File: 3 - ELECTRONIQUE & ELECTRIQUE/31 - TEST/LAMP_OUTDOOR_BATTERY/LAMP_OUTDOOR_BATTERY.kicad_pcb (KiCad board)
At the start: 2 copper layers, 15.3 x 61.6 mm, 13 parts, among them J1 629722000214, U1 MCP73833-FCI_UN, U2 MT3608

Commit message: Commit_1.02 Modification shape PCB
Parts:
- C1, C2: footprint Capacitor_SMD:C_0805_2012Metric_Pad1.18x1.45mm_HandSolder -> Capacitor_SMD:C_0402_1005Metric_Pad0.74x0.62mm_HandSolder
- R1, R2, R3, R4, R5: footprint Resistor_SMD:R_0805_2012Metric_Pad1.20x1.40mm_HandSolder -> Resistor_SMD:R_0402_1005Metric_Pad0.72x0.64mm_HandSolder
- moved C1 45.7 mm to (187.9, 79.4)
- moved C2 45.7 mm to (187.9, 82.4)
- moved D1 45.7 mm to (183.2, 79.4)
- moved D2 45.7 mm to (183.2, 82.4)
- moved D3 45.7 mm to (183.2, 85.5)
- moved U1 45.7 mm to (186.2, 74.4)
- moved R1 45.3 mm to (187.6, 104.4)
- moved R2 45.3 mm to (187.6, 107.4)
- moved R3 45.3 mm to (187.6, 110.3)
- moved R4 45.3 mm to (187.6, 113.3)
- moved R5 45.3 mm to (187.6, 116.2)
- moved U2 45.3 mm to (185.1, 99.8)
- moved J1 41.5 mm to (170.5, 91.5)
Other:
- board size 15.3 x 61.6 mm -> 24.5 x 67.8 mm

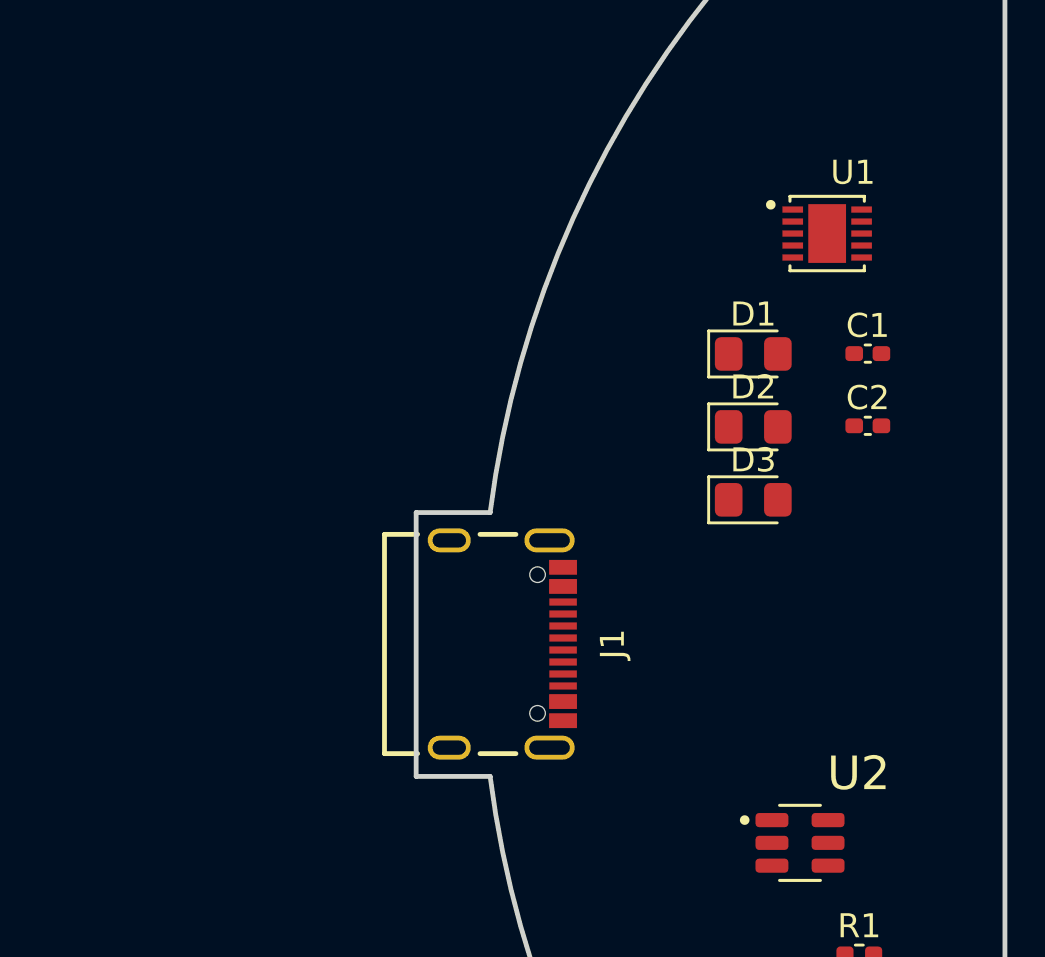
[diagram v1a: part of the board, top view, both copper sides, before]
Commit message: Boost converter circuit
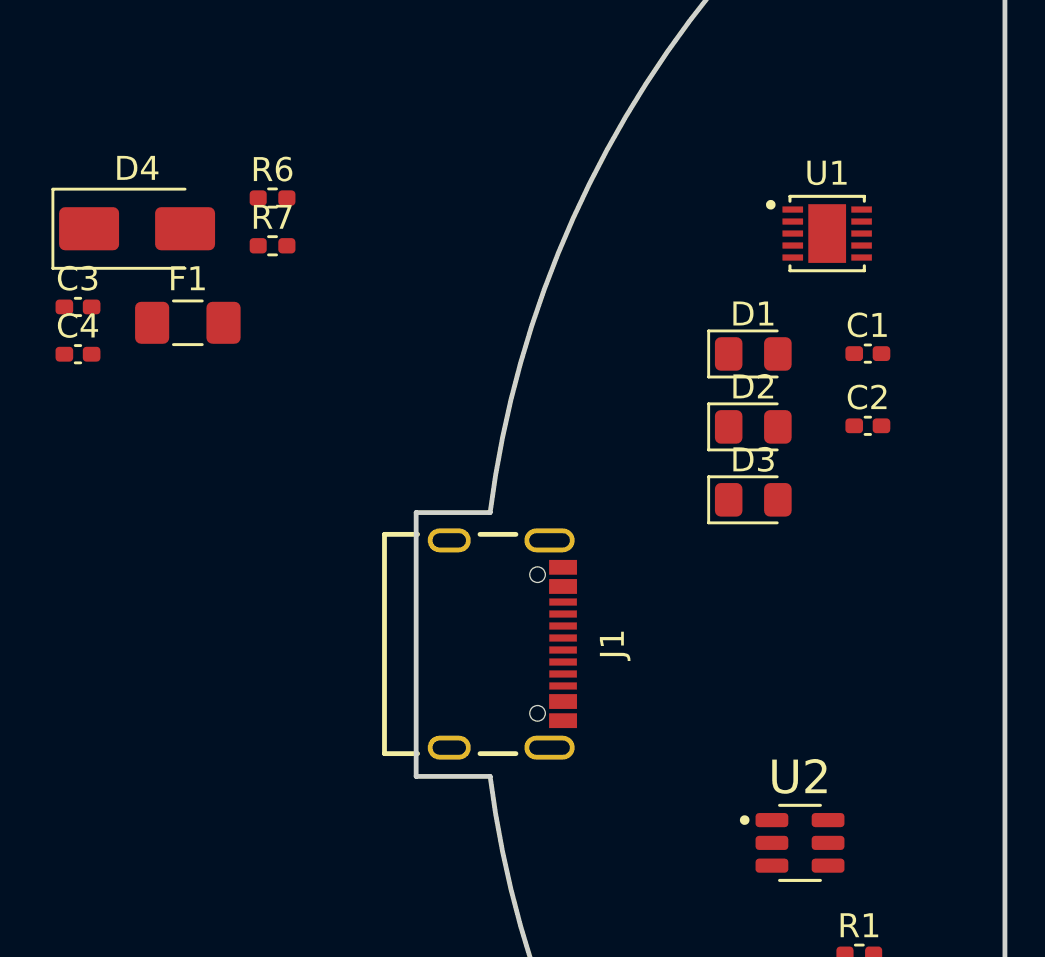
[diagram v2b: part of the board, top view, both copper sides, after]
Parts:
- added C3: 22uF, Capacitor_SMD:C_0402_1005Metric_Pad0.74x0.62mm_HandSolder, F.Cu at (155.0, 77.4)
- added C4: 22uF, Capacitor_SMD:C_0402_1005Metric_Pad0.74x0.62mm_HandSolder, F.Cu at (155.0, 79.4)
- added D4: SS24, Diode_SMD:D_SMA, F.Cu at (157.5, 74.2)
- added F1: Fuse_Small, Fuse:Fuse_1206_3216Metric_Pad1.42x1.75mm_HandSolder, F.Cu at (159.6, 78.1)
- added R6: 110K, Resistor_SMD:R_0402_1005Metric_Pad0.72x0.64mm_HandSolder, F.Cu at (163.1, 72.9)
- added R7: 15K, Resistor_SMD:R_0402_1005Metric_Pad0.72x0.64mm_HandSolder, F.Cu at (163.1, 74.9)
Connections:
- U2 pad 1: unconnected-(U2-SW-Pad1) -> Net-(D4-A)
- U2 pad 2: unconnected-(U2-GND-Pad2) -> GND
- U2 pad 3: unconnected-(U2-FB-Pad3) -> Net-(U2-FB)
- U2 pad 5: unconnected-(U2-IN-Pad5) -> +BATT

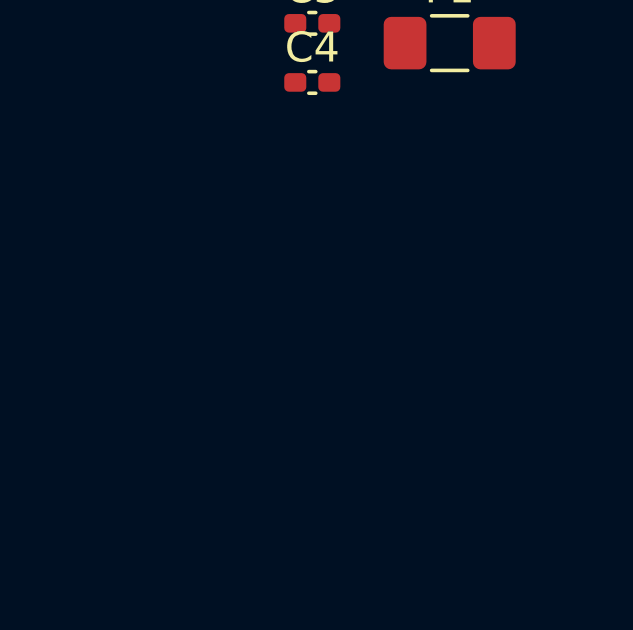
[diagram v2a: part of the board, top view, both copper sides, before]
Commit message: Import des symboles et empreintes
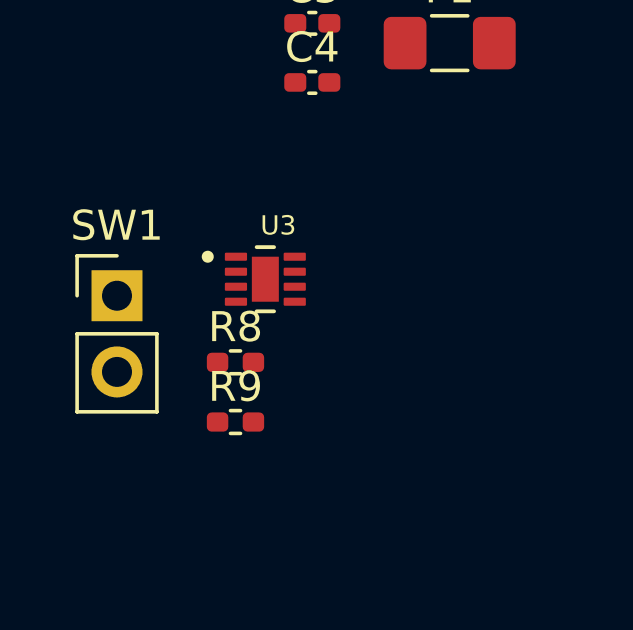
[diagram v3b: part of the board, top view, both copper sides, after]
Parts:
- added R8: 10K, Resistor_SMD:R_0402_1005Metric_Pad0.72x0.64mm_HandSolder, F.Cu at (152.4, 88.7)
- added R9: 10K, Resistor_SMD:R_0402_1005Metric_Pad0.72x0.64mm_HandSolder, F.Cu at (152.4, 90.7)
- added SW1: SW_SPST, Connector_PinHeader_2.54mm:PinHeader_1x02_P2.54mm_Vertical, F.Cu at (148.5, 86.5)
- added U3: AT42QT1012-MAHR, LAMP_OUTDOOR_BATTERY:SON50P200X200X60-9N, F.Cu at (153.4, 86.0)
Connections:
- net Net-(D4-A) renamed /SW
- net Net-(U2-FB) renamed /V_FB
- C3 pad 2: +BATT -> /IN
- F1 pad 1: +BATT -> Net-(BT1-+)
- F1 pad 2: BatteryPole+ -> +BATT
- U2 pad 4: unconnected-(U2-EN-Pad4) -> TS
- U2 pad 5: +BATT -> /IN

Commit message: Conception schéma suite
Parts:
- added C5: ~, Capacitor_SMD:C_0402_1005Metric_Pad0.74x0.62mm_HandSolder, F.Cu at (112.1, 73.0)
- added C6: 0.1uF, Capacitor_SMD:C_0402_1005Metric_Pad0.74x0.62mm_HandSolder, F.Cu at (112.1, 75.0)
- added J2: Batt+, LAMP_OUTDOOR_BATTERY:BatteryPole, F.Cu at (157.6, 60.3)
- added J3: Batt-, LAMP_OUTDOOR_BATTERY:BatteryPole, F.Cu at (157.6, 113.7)
- added L1: 4.7uH, Inductor_SMD:L_0805_2012Metric_Pad1.15x1.40mm_HandSolder, F.Cu at (129.5, 105.5)
- added R10: ~, Resistor_SMD:R_0402_1005Metric_Pad0.72x0.64mm_HandSolder, F.Cu at (108.9, 73.0)
- added R11: ~, Resistor_SMD:R_0402_1005Metric_Pad0.72x0.64mm_HandSolder, F.Cu at (108.9, 75.0)
- added R12: 100k, Resistor_SMD:R_0402_1005Metric_Pad0.72x0.64mm_HandSolder, F.Cu at (108.9, 77.0)
- added R13: 0, Resistor_SMD:R_0402_1005Metric_Pad0.72x0.64mm_HandSolder, F.Cu at (117.9, 63.4)
- moved U3 52.8 mm to (103.9, 104.0)
- moved D3 43.9 mm to (145.8, 108.7), turned to 90 degrees
- moved D2 43.5 mm to (145.8, 104.7), turned to 90 degrees
- moved D1 43.0 mm to (145.8, 100.8), turned to 90 degrees
- moved C1 41.1 mm to (148.4, 90.6), turned to -90 degrees
- moved R5 39.9 mm to (155.6, 92.3)
- moved U2 39.6 mm to (151.8, 78.4)
- moved U1 39.0 mm to (151.4, 91.9)
- moved R1 38.3 mm to (150.2, 96.0), turned to 90 degrees
- moved R2 37.9 mm to (151.4, 96.0), turned to 90 degrees
- moved R3 37.8 mm to (152.6, 96.0), turned to 90 degrees
- moved R4 37.6 mm to (155.6, 93.4)
- moved C2 34.4 mm to (154.5, 90.6), turned to -90 degrees
- moved D4 32.3 mm to (125.2, 74.6)
- moved R6 32.3 mm to (130.8, 73.3)
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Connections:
- F1 pad 1: Net-(BT1-+) -> /Battery+
- R8 pad 1: TS -> /EN
- R9 pad 2: TS -> /EN
- U2 pad 4: TS -> /EN
- U3 pad 1: unconnected-(U3-SNSK-Pad1) -> Net-(U3-SNSK)
- U3 pad 4: unconnected-(U3-VSS-Pad4) -> GND
- U3 pad 5: unconnected-(U3-OUT-Pad5) -> TS
- U3 pad 6: unconnected-(U3-TIME-Pad6) -> GND
- U3 pad 7: unconnected-(U3-VDD-Pad7) -> +5V
- U3 pad 8: unconnected-(U3-SNS-Pad8) -> Net-(U3-SNS)
- U3 pad 9: unconnected-(U3-EXP-Pad9) -> GND
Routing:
- net Net-(U1-STAT1): track 0.00 -> 5.17 mm
- net Net-(U1-STAT2): track 0.00 -> 4.83 mm
- net Net-(U1-~{PG}): track 0.00 -> 4.49 mm, vias 0 -> 2
- net Net-(U1-THERM): track 0.00 -> 2.29 mm
- net Net-(U1-PROG): track 0.00 -> 1.95 mm
- net GND: vias 0 -> 1
- added copper zone on F.Cu, net +5V
- added copper zone on F.Cu, net +BATT
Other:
- board size 24.5 x 67.8 mm -> 24 x 68.3 mm

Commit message: Conception PCB suite
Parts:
- removed F1: Fuse_Small, Fuse:Fuse_1206_3216Metric_Pad1.42x1.75mm_HandSolder
- added ? (x2): , , F.Cu at (157.8, 123.1)
- added C7: 0.1uF, Capacitor_SMD:C_0402_1005Metric_Pad0.74x0.62mm_HandSolder, F.Cu at (149.4, 83.6)
- added J4: Led+, LAMP_OUTDOOR_BATTERY:BatteryPole, F.Cu at (157.4, 110.5)
- added J5: Led-, LAMP_OUTDOOR_BATTERY:BatteryPole, F.Cu at (157.4, 114.5)
- added J6: Electrode Sensor, LAMP_OUTDOOR_BATTERY:BatteryPole, F.Cu at (165.4, 86.1)
- added Q1: IRLML6344, Package_TO_SOT_SMD:SOT-23-3, F.Cu at (146.0, 79.6)
- added Q2: IRLML6344, Package_TO_SOT_SMD:SOT-23-3, F.Cu at (146.0, 83.4)
- added R14: 2.2K, Resistor_SMD:R_0402_1005Metric_Pad0.72x0.64mm_HandSolder, F.Cu at (149.3, 79.3)
- added R15: 330, Resistor_SMD:R_0402_1005Metric_Pad0.72x0.64mm_HandSolder, F.Cu at (151.3, 83.0)
- added REF**: MountingHole_2.7mm_M2.5_DIN965_Pad_TopBottom, MountingHole:MountingHole_2.7mm_M2.5_DIN965_Pad_TopBottom, F.Cu at (157.8, 123.1)
- added REF**: MountingHole_2.7mm_M2.5_DIN965_Pad_TopBottom, MountingHole:MountingHole_2.7mm_M2.5_DIN965_Pad_TopBottom, F.Cu at (157.8, 60.8)
- added U4: BQ29737DSER, Package_SON:WSON-6_1.5x1.5mm_P0.5mm, F.Cu at (149.3, 81.6)
- J2, J3: moved to B.Cu
- moved U3 70.2 mm to (172.5, 89.1)
- moved R10 61.9 mm to (170.5, 79.2)
- moved R11 61.9 mm to (170.5, 81.2)
- moved R12 61.9 mm to (170.5, 83.2)
- moved C5 61.9 mm to (173.7, 79.2)
- moved C6 61.9 mm to (173.7, 81.2)
- moved R13 60.2 mm to (164.7, 101.2), turned to 180 degrees
- moved D4 46.6 mm to (152.3, 112.5), turned to -90 degrees
- moved C4 43.8 mm to (157.4, 106.7)
- moved R6 41.6 mm to (157.4, 105.4), turned to 180 degrees
- moved R7 39.2 mm to (157.4, 104.1)
- moved C3 39.1 mm to (150.1, 105.7), turned to 90 degrees
- moved R9 34.4 mm to (152.7, 102.3), turned to 180 degrees
- moved R8 33.1 mm to (150.2, 103.3), turned to -90 degrees
- moved U2 26.7 mm to (153.3, 105.1), turned to 180 degrees
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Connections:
- J2 pad 1: /Battery+ -> +BATT
- J3 pad 1: GND -> /Battery-
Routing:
- net +BATT: track 0.00 -> 45.5 mm, vias 0 -> 4
- net /Battery-: track 0.00 -> 44.6 mm, vias 0 -> 4
- net +5V: track 0.00 -> 21.5 mm, vias 0 -> 3
- net Net-(D3-K): track 0.00 -> 19.5 mm
- net Net-(D2-K): track 0.00 -> 13.2 mm
- net /SW: track 0.00 -> 8.91 mm
- net Net-(D1-K): track 0.00 -> 8.88 mm
- net /Led_V+: track 0.00 -> 7.26 mm
- net Net-(Q2-G): track 0.00 -> 6.11 mm
- net /EN: track 0.00 -> 3.89 mm
- net /V_FB: track 0.00 -> 3.64 mm
- net Net-(U4-V-): track 0.00 -> 3.13 mm
- net Net-(U4-BAT): track 0.00 -> 3.09 mm
- net Net-(Q1-G): track 0.00 -> 2.88 mm
- net Net-(U1-THERM): track 2.29 -> 4.92 mm
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- added copper zone on B.Cu, net +BATT
- added copper zone on B.Cu, net /Battery-
- added copper zone on F.Cu, net /Battery-
- added copper zone on F.Cu, net /IN
- added copper zone on F.Cu, net /Led_V+
- added copper zone on F.Cu, net /SW
- added copper zone on F.Cu, net Net-(Q1-D)
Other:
- outline, holes or cut-outs redrawn

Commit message: PCB & Conception 3D V1
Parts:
- J2, J3: moved to F.Cu
- L1: footprint Inductor_SMD:L_0805_2012Metric_Pad1.15x1.40mm_HandSolder -> LAMP_OUTDOOR_BATTERY:IND_F1C1-201608-4R7M
- moved C6 19.9 mm to (153.9, 80.1)
- moved U3 18.5 mm to (156.8, 79.5), turned to 180 degrees
- moved R12 17.2 mm to (153.9, 78.8), turned to 180 degrees
- moved C5 17.0 mm to (156.8, 81.4)
- moved R11 14.9 mm to (155.7, 82.6), turned to 180 degrees
- moved R10 12.7 mm to (158.2, 82.6)
- moved R13 11.3 mm to (153.7, 98.9), turned to -90 degrees
- moved J6 8.51 mm to (156.9, 85.0)
- moved D4 1.00 mm to (152.3, 111.5)
- moved J4 1.00 mm to (157.4, 109.5)
- moved J5 1.00 mm to (157.4, 113.5)
- turned J2 to 0 degrees
- turned J3 to 0 degrees
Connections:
- C6 pad 2: +5V -> +BATT
- U3 pad 7: +5V -> +BATT
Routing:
- net TS: track 0.00 -> 24.2 mm
- net +BATT: track 45.5 -> 53.9 mm, vias 4 -> 8
- net /Battery-: track 44.6 -> 49.0 mm, vias 4 -> 6
- net /EN: track 3.89 -> 7.55 mm
- net Net-(U3-SNSK): track 0.00 -> 3.24 mm
- net /ElecSensor: track 0.00 -> 2.64 mm
- net Net-(U3-SNS): track 0.00 -> 2.56 mm
- net /SW: track 8.91 -> 7.71 mm
- net GND: vias 20 -> 42
- added copper zone on B.Cu, net GND
- added copper zone on F.Cu, net GND
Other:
- board text added: "Batt+"
- board text added: "Batt-"
- board text added: "Battery 18650"
- board text added: "Electrode"
- board text added: "Fanovard Arnaud"
- board text added: "Lamp Outdoor"
- board text added: "Led+"
- board text added: "Led-"
- board text added: "V1.0"
